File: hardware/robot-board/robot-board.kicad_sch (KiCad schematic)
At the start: 131 parts, among them J1 Conn_01x09_Pin, J10 1x2_Screw, J11 1x2_Screw, J2 Barrel_Jack, J3 USB_C_Receptacle_USB2.0_14P, J4 Conn_01x03_Pin, J5 Conn_01x03_Pin, J6 Conn_01x03_Pin, J7 Conn_01x03_Pin, J8 1x2_Screw, J9 1x2_Screw, Q1 BSS138, Q2 BSS138, Q3 BSS138, Q4 BSS138, Q5 BSS138, SW1 SW_SPST, SW2 SW_SPST, SW3 SW_SPST, U1 ESP32-S3-WROOM-1, U10 MAX7219, U2 LMR51450, U3 LMR51450, U4 TVS1400DRV, U6 DRV8835, U7 DRV8835, U8 XL-SA3391SRWC, U9 74AHCT125

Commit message: fixed fuse holder
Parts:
- F1: footprint Fuse:Fuse_Littelfuse-NANO2-451_453 -> Fuse:Fuseholder_Littelfuse_Nano2_154x; JLC P/N C178991 -> C206916
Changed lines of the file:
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@@
 			)
 		)
-		(property "Footprint" "Fuse:Fuse_Littelfuse-NANO2-451_453"
+		(property "Footprint" "Fuse:Fuseholder_Littelfuse_Nano2_154x"
 			(at 147.32 128.27 0)
 			(hide yes)
@@
 			)
 		)
-		(property "JLC P/N" "C178991"
+		(property "JLC P/N" "C206916"
 			(at 147.32 128.27 0)
 			(hide yes)

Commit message: changed to screw terminals
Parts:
- J10, J11, J8, J9: footprint footprints:CONN2_2060-452&slash_998-404_WAG -> footprints:TerminalBlock_DB301V-3.5-2P-GN-H_1x02_P3.50mm_Horizontal
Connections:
- net M0+: now also J10.2 (Pin_2), U7.3 (A_OUT2); no longer J8.2 (Pin_2), U6.3 (A_OUT2)
- net M0-: now also J10.1 (Pin_1), U7.2 (A_OUT1); no longer J8.1 (Pin_1), U6.2 (A_OUT1)
- net M1+: now also J11.2 (Pin_2), U7.5 (B_OUT2); no longer J9.2 (Pin_2), U6.5 (B_OUT2)
- net M1-: now also J11.1 (Pin_1), U7.4 (B_OUT1); no longer J9.1 (Pin_1), U6.4 (B_OUT1)
- net M2+: now also J8.2 (Pin_2), U6.3 (A_OUT2); no longer J10.2 (Pin_2), U7.3 (A_OUT2)
- net M2-: now also J8.1 (Pin_1), U6.2 (A_OUT1); no longer J10.1 (Pin_1), U7.2 (A_OUT1)
- net M3+: now also J9.2 (Pin_2), U6.5 (B_OUT2); no longer J11.2 (Pin_2), U7.5 (B_OUT2)
- net M3-: now also J9.1 (Pin_1), U6.4 (B_OUT1); no longer J11.1 (Pin_1), U7.4 (B_OUT1)
- net MOTOR0_EN: now also U1.22 (IO14), U7.9 (A_EN); no longer U1.29 (IO36), U6.9 (A_EN)
- net MOTOR0_PHASE: now also U1.17 (IO9), U7.10 (A_PH); no longer U1.7 (IO7), U6.10 (A_PH)
- net MOTOR1_EN: now also U1.37 (TXD0), U7.7 (B_EN); no longer U1.28 (IO35), U6.7 (B_EN)
- net MOTOR1_PHASE: now also U1.18 (IO10), U7.8 (B_PH); no longer U1.12 (IO8), U6.8 (B_PH)
- net MOTOR2_EN: now also U1.29 (IO36), U6.9 (A_EN); no longer U1.22 (IO14), U7.9 (A_EN)
- net MOTOR2_PHASE: now also U1.7 (IO7), U6.10 (A_PH); no longer U1.17 (IO9), U7.10 (A_PH)
- net MOTOR3_EN: now also U1.28 (IO35), U6.7 (B_EN); no longer U1.37 (TXD0), U7.7 (B_EN)
- net MOTOR3_PHASE: now also U1.12 (IO8), U6.8 (B_PH); no longer U1.18 (IO10), U7.8 (B_PH)
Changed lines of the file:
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@@
 		)
 	)
-	(label "MOTOR3_PHASE"
+	(label "MOTOR1_PHASE"
 		(at 255.27 114.3 0)
 		(effects
@@
 		)
 	)
-	(label "M1+"
+	(label "M3+"
 		(at 302.26 87.63 0)
 		(effects
@@
 		)
 	)
-	(label "MOTOR2_EN"
+	(label "MOTOR0_EN"
 		(at 255.27 111.76 0)
 		(effects
@@
 		)
 	)
-	(label "MOTOR2_PHASE"
+	(label "MOTOR0_PHASE"
 		(at 255.27 109.22 0)
 		(effects
@@
 		)
 	)
-	(label "M1-"
+	(label "M3-"
 		(at 294.64 85.09 180)
 		(effects
@@
 		)
 	)
-	(label "MOTOR1_PHASE"
+	(label "MOTOR3_PHASE"
 		(at 255.27 87.63 0)
 		(effects
@@
 		)
 	)
-	(label "M2+"
+	(label "M0+"
 		(at 302.26 107.95 0)
 		(effects
@@
 		)
 	)
-	(label "M0+"
+	(label "M2+"
 		(at 294.64 82.55 180)
 		(effects
@@
 		)
 	)
-	(label "M3-"
+	(label "M1-"
 		(at 302.26 111.76 0)
 		(effects
@@
 		)
 	)
-	(label "M0-"
+	(label "M2-"
 		(at 302.26 78.74 0)
 		(effects
@@
 		)
 	)
-	(label "M1-"
+	(label "M3-"
 		(at 302.26 85.09 0)
 		(effects
@@
 		)
 	)
-	(label "MOTOR0_EN"
+	(label "MOTOR2_EN"
 		(at 255.27 85.09 0)
 		(effects
@@
 		)
 	)
-	(label "M1+"
+	(label "M3+"
 		(at 294.64 87.63 180)
 		(effects
@@
 		)
 	)
-	(label "MOTOR0_PHASE"
+	(label "MOTOR2_PHASE"
 		(at 255.27 82.55 0)
 		(effects
@@
 		)
 	)
-	(label "M3+"
+	(label "M1+"
 		(at 302.26 114.3 0)
 		(effects
@@
 		)
 	)
-	(label "M2+"
+	(label "M0+"
 		(at 294.64 109.22 180)
 		(effects
@@
 		)
 	)
-	(label "MOTOR1_EN"
+	(label "MOTOR3_EN"
 		(at 255.27 90.17 0)
 		(effects
@@
 		)
 	)
-	(label "MOTOR0_EN"
+	(label "MOTOR2_EN"
 		(at 82.55 57.15 180)
 		(effects
@@
 		)
 	)
-	(label "M3-"
+	(label "M1-"
 		(at 294.64 111.76 180)
 		(effects
@@
 		)
 	)
-	(label "MOTOR1_PHASE"
+	(label "MOTOR3_PHASE"
 		(at 24.13 62.23 0)
 		(effects
@@
 		)
 	)
-	(label "M2-"
+	(label "M0-"
 		(at 302.26 105.41 0)
 		(effects
@@
 		)
 	)
-	(label "MOTOR2_EN"
+	(label "MOTOR0_EN"
 		(at 24.13 77.47 0)
 		(effects
@@
 		)
 	)
-	(label "M0-"
+	(label "M2-"
 		(at 294.64 80.01 180)
 		(effects
@@
 		)
 	)
-	(label "MOTOR3_PHASE"
+	(label "MOTOR1_PHASE"
 		(at 24.13 67.31 0)
 		(effects
@@
 		)
 	)
-	(label "M3+"
+	(label "M1+"
 		(at 294.64 114.3 180)
 		(effects
@@
 		)
 	)
-	(label "MOTOR3_EN"
+	(label "MOTOR1_EN"
 		(at 82.55 36.83 180)
 		(effects
@@
 		)
 	)
-	(label "M2-"
+	(label "M0-"
 		(at 294.64 106.68 180)
 		(effects
@@
 		)
 	)
-	(label "MOTOR0_PHASE"
+	(label "MOTOR2_PHASE"
 		(at 24.13 59.69 0)
 		(effects
@@
 		)
 	)
-	(label "M0+"
+	(label "M2+"
 		(at 302.26 81.28 0)
 		(effects
@@
 		)
 	)
-	(label "MOTOR3_EN"
+	(label "MOTOR1_EN"
 		(at 255.27 116.84 0)
 		(effects
@@
 		)
 	)
-	(label "MOTOR2_PHASE"
+	(label "MOTOR0_PHASE"
 		(at 24.13 64.77 0)
 		(effects
@@
 		)
 	)
-	(label "MOTOR1_EN"
+	(label "MOTOR3_EN"
 		(at 82.55 54.61 180)
 		(effects
@@
 			)
 		)
-		(property "Footprint" "footprints:CONN2_2060-452&slash_998-404_WAG"
+		(property "Footprint" "footprints:TerminalBlock_DB301V-3.5-2P-GN-H_1x02_P3.50mm_Horizontal"
 			(at 312.42 105.41 0)
 			(hide yes)
@@
 			)
 		)
-		(property "Footprint" "footprints:CONN2_2060-452&slash_998-404_WAG"
+		(property "Footprint" "footprints:TerminalBlock_DB301V-3.5-2P-GN-H_1x02_P3.50mm_Horizontal"
 			(at 312.42 111.76 0)
 			(hide yes)
@@
 			)
 		)
-		(property "Footprint" "footprints:CONN2_2060-452&slash_998-404_WAG"
+		(property "Footprint" "footprints:TerminalBlock_DB301V-3.5-2P-GN-H_1x02_P3.50mm_Horizontal"
 			(at 312.42 85.09 0)
 			(hide yes)
@@
 			)
 		)
-		(property "Footprint" "footprints:CONN2_2060-452&slash_998-404_WAG"
+		(property "Footprint" "footprints:TerminalBlock_DB301V-3.5-2P-GN-H_1x02_P3.50mm_Horizontal"
 			(at 312.42 78.74 0)
 			(hide yes)

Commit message: small spacing changes, renamed motor lines
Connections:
- net BS: now also R44.2, SW2.1 (A)
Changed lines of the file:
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@@
 	)
 	(label "BS"
-		(at 173.99 200.66 0)
+		(at 217.17 200.66 0)
 		(effects
 			(font

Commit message: Replaced net-ties with thinner versions; separated AGND nets
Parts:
- NT1, NT2: footprint NetTie:NetTie-2_SMD_Pad0.5mm -> footprints:NetTie-2_SMD_Pad0.25mm
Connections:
- net AGND renamed AGND_3V3
- net AGND_3V3: no longer NT2.1, R5.2, U3.8 (AGND)
- new net AGND_5V: NT2.1, R5.2, U3.8 (AGND)
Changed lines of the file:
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@@
 			)
 		)
-		(property "Value" "AGND"
+		(property "Value" "AGND_3V3"
 			(at 82.55 149.86 0)
 			(show_name no)
@@
 			)
 		)
-		(property "Value" "AGND"
+		(property "Value" "AGND_3V3"
 			(at 22.86 151.13 0)
 			(show_name no)
@@
 			)
 		)
-		(property "Value" "AGND"
+		(property "Value" "AGND_5V"
 			(at 82.55 191.77 0)
 			(show_name no)
@@
 			)
 		)
-		(property "Value" "AGND"
+		(property "Value" "AGND_5V"
 			(at 22.86 191.77 0)
 			(show_name no)
@@
 			)
 		)
-		(property "Footprint" "NetTie:NetTie-2_SMD_Pad0.5mm"
+		(property "Footprint" "footprints:NetTie-2_SMD_Pad0.25mm"
 			(at 26.67 186.69 0)
 			(hide yes)
@@
 			)
 		)
-		(property "Footprint" "NetTie:NetTie-2_SMD_Pad0.5mm"
+		(property "Footprint" "footprints:NetTie-2_SMD_Pad0.25mm"
 			(at 26.67 146.05 0)
 			(hide yes)

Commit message: updated bom; added screw terminal JLC part #
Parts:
- J10, J11, J8, J9: JLC P/N C2765055 -> C695629
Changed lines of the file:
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@@
 			)
 		)
-		(property "JLC P/N" "C2765055"
+		(property "JLC P/N" "C695629"
 			(at 312.42 105.41 0)
 			(hide yes)
@@
 			)
 		)
-		(property "JLC P/N" "C2765055"
+		(property "JLC P/N" "C695629"
 			(at 312.42 111.76 0)
 			(hide yes)
@@
 			)
 		)
-		(property "JLC P/N" "C2765055"
+		(property "JLC P/N" "C695629"
 			(at 312.42 85.09 0)
 			(hide yes)
@@
 			)
 		)
-		(property "JLC P/N" "C2765055"
+		(property "JLC P/N" "C695629"
 			(at 312.42 78.74 0)
 			(hide yes)

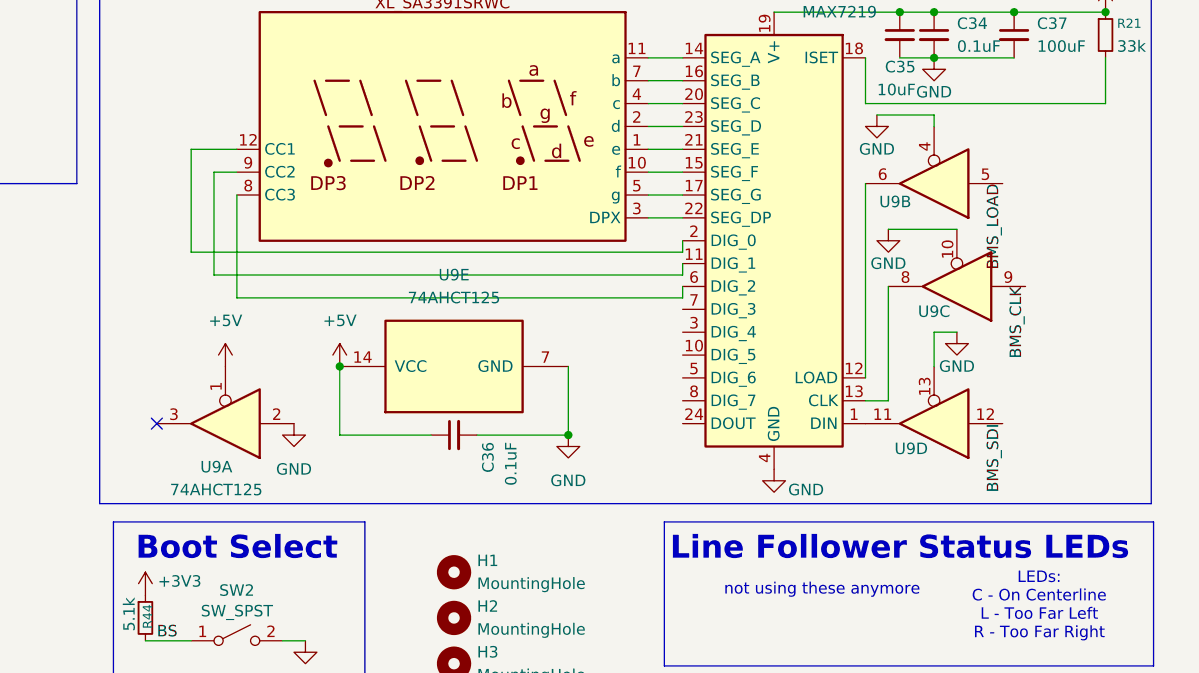
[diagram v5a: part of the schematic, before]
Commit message: changed 74AHCT125PWR for SN74ACT125PWR
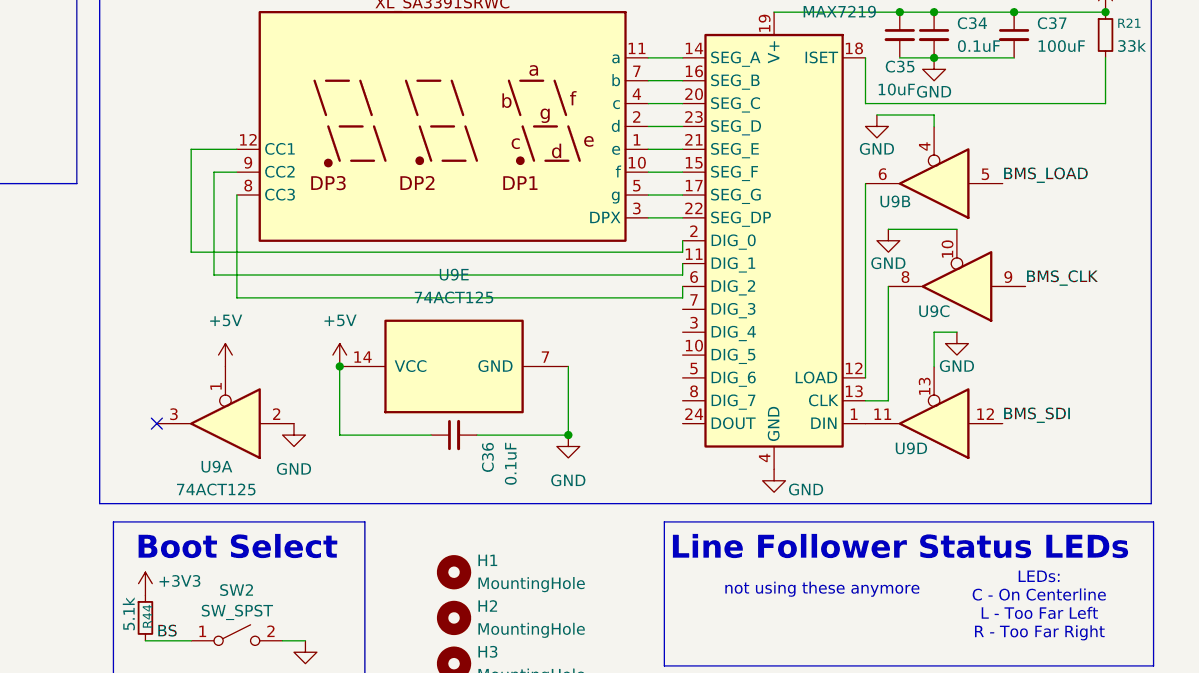
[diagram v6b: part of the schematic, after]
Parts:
- U9: value 74AHCT125 -> 74ACT125; symbol 74xx:74AHCT125 -> robot-board-library:74ACT125; JLC P/N C36365 -> C52940839
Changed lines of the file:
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@@
 	)
 	(label "BMS_LOAD"
-		(at 311.15 149.86 270)
+		(at 311.15 149.86 0)
 		(effects
 			(font
 				(size 1.27 1.27)
 			)
-			(justify right bottom)
+			(justify left bottom)
 		)
 	)
@@
 	)
 	(label "BMS_CLK"
-		(at 313.69 161.29 270)
+		(at 313.69 161.29 0)
 		(effects
 			(font
 				(size 1.27 1.27)
 			)
-			(justify right bottom)
+			(justify left bottom)
 		)
 	)
@@
 	)
 	(label "BMS_SDI"
-		(at 311.15 176.53 270)
+		(at 311.15 176.53 0)
 		(effects
 			(font
 				(size 1.27 1.27)
 			)
-			(justify right bottom)
+			(justify left bottom)
 		)
 	)
@@
 	)
 	(symbol
-		(lib_id "74xx:74AHCT125")
+		(lib_id "robot-board-library:74ACT125")
 		(at 224.79 176.53 180)
 		(unit 1)
@@
 			)
 		)
-		(property "Value" "74AHCT125"
+		(property "Value" "74ACT125"
 			(at 223.774 183.896 0)
 			(show_name no)
@@
 			)
 		)
-		(property "Datasheet" "https://www.ti.com/lit/ds/symlink/sn74ahct125.pdf"
+		(property "Datasheet" "https://www.ti.com/lit/ds/symlink/sn74act125.pdf"
 			(at 224.79 176.53 0)
 			(hide yes)
@@
 			)
 		)
-		(property "JLC P/N" "C36365"
+		(property "JLC P/N" "C52940839"
 			(at 224.79 176.53 0)
 			(hide yes)
@@
 	)
 	(symbol
-		(lib_id "74xx:74AHCT125")
+		(lib_id "robot-board-library:74ACT125")
 		(at 303.53 176.53 180)
 		(unit 4)
@@
 			)
 		)
-		(property "Value" "74AHCT125"
+		(property "Value" "74ACT125"
 			(at 300.99 181.864 0)
 			(hide yes)
@@
 			)
 		)
-		(property "Datasheet" "https://www.ti.com/lit/ds/symlink/sn74ahct125.pdf"
+		(property "Datasheet" "https://www.ti.com/lit/ds/symlink/sn74act125.pdf"
 			(at 303.53 176.53 0)
 			(hide yes)
@@
 			)
 		)
-		(property "JLC P/N" "C36365"
+		(property "JLC P/N" "C52940839"
 			(at 303.53 176.53 0)
 			(hide yes)
@@
 	)
 	(symbol
-		(lib_id "74xx:74AHCT125")
+		(lib_id "robot-board-library:74ACT125")
 		(at 250.19 170.18 90)
 		(unit 5)
@@
 			)
 		)
-		(property "Value" "74AHCT125"
+		(property "Value" "74ACT125"
 			(at 250.19 162.56 90)
 			(show_name no)
@@
 			)
 		)
-		(property "Datasheet" "https://www.ti.com/lit/ds/symlink/sn74ahct125.pdf"
+		(property "Datasheet" "https://www.ti.com/lit/ds/symlink/sn74act125.pdf"
 			(at 250.19 170.18 0)
 			(hide yes)
@@
 			)
 		)
-		(property "JLC P/N" "C36365"
+		(property "JLC P/N" "C52940839"
 			(at 250.19 170.18 90)
 			(hide yes)
@@
 	)
 	(symbol
-		(lib_id "74xx:74AHCT125")
+		(lib_id "robot-board-library:74ACT125")
 		(at 303.53 149.86 180)
 		(unit 2)
@@
 			)
 		)
-		(property "Value" "74AHCT125"
+		(property "Value" "74ACT125"
 			(at 299.212 154.432 0)
 			(hide yes)
@@
 			)
 		)
-		(property "Datasheet" "https://www.ti.com/lit/ds/symlink/sn74ahct125.pdf"
+		(property "Datasheet" "https://www.ti.com/lit/ds/symlink/sn74act125.pdf"
 			(at 303.53 149.86 0)
 			(hide yes)
@@
 			)
 		)
-		(property "JLC P/N" "C36365"
+		(property "JLC P/N" "C52940839"
 			(at 303.53 149.86 0)
 			(hide yes)
@@
 	)
 	(symbol
-		(lib_id "74xx:74AHCT125")
+		(lib_id "robot-board-library:74ACT125")
 		(at 306.07 161.29 180)
 		(unit 3)
@@
 			)
 		)
-		(property "Value" "74AHCT125"
+		(property "Value" "74ACT125"
 			(at 303.53 166.624 0)
 			(hide yes)
@@
 			)
 		)
-		(property "Datasheet" "https://www.ti.com/lit/ds/symlink/sn74ahct125.pdf"
+		(property "Datasheet" "https://www.ti.com/lit/ds/symlink/sn74act125.pdf"
 			(at 306.07 161.29 0)
 			(hide yes)
@@
 			)
 		)
-		(property "JLC P/N" "C36365"
+		(property "JLC P/N" "C52940839"
 			(at 306.07 161.29 0)
 			(hide yes)
